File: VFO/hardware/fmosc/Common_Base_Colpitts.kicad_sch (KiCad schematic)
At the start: 28 parts, among them J5 JST PH, J6 3670128, J7 U.FL, Q5 MMBT5179, Q6 MMBT5179, Q7 MMBT5179

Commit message: R1 for generating gerber
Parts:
- removed C16: 10n, g-cap:C_0603_1608Metric, symbol #gplm:cap/CAP-0000-0103
- removed J6: 3670128, g-rfm:H_Wurth_WE-SHC-SEAMLESS-FRAME_3670128, symbol #gplm:rfm/RFM-0000-0001
- added C19: 10n, g-cap:C_0603_1608Metric, symbol #gplm:cap/CAP-0000-0103
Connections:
- net +5V: now also C19.1
- net GND: now also C19.2
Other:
- moved on the sheet: C14, J5, R20

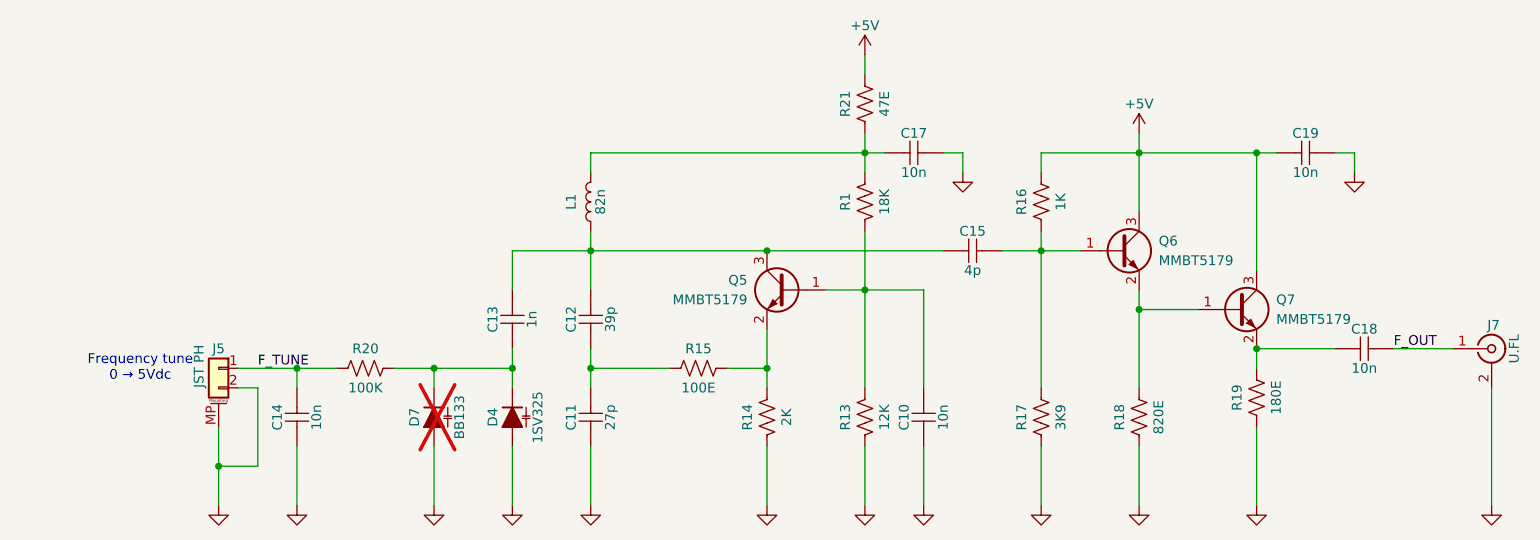
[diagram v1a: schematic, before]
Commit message: Adding DC voltages to the schematic + updating from libraries
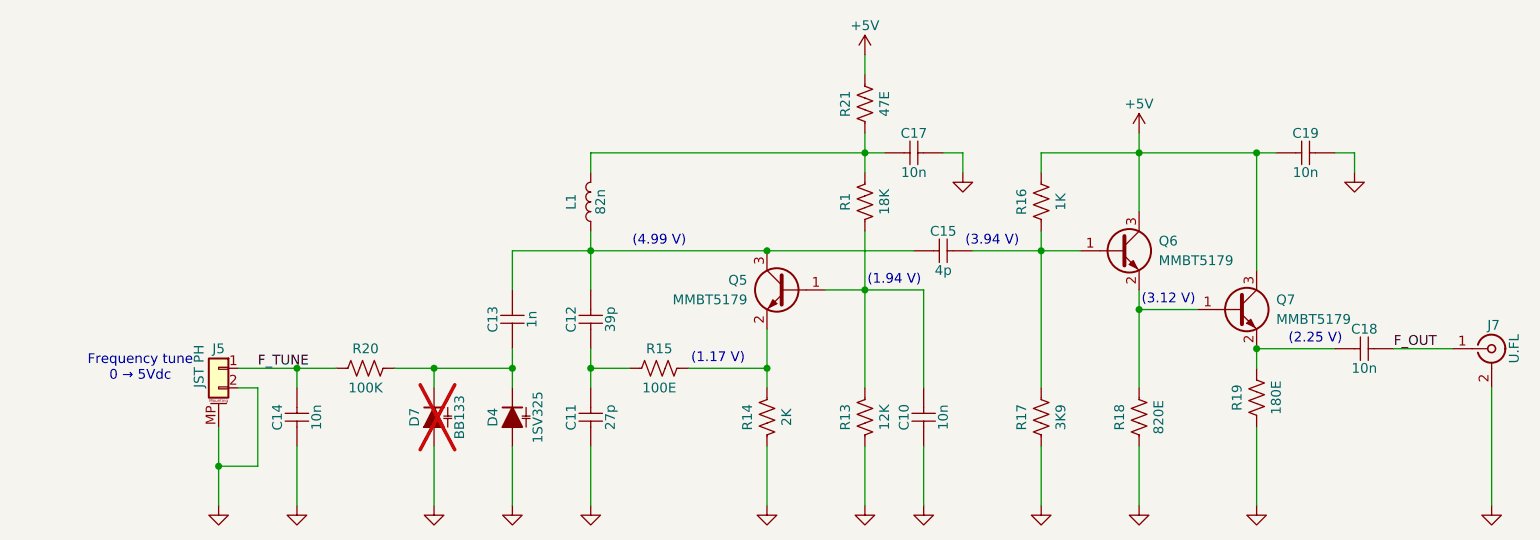
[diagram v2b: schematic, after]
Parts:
- L1: symbol #gplm:ind/IND-0000-0820 -> #gplm:ind/IND-0001-0820; Current 2.5A -> 2.5; IPN IND-0000-0820 -> IND-0001-0820
- Q5, Q6, Q7: max(Ic) 50m -> 0.05
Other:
- note added: "(1.17 V)"
- note added: "(1.94 V)"
- note added: "(2.25 V)"
- note added: "(3.12 V)"
- note added: "(3.94 V)"
- note added: "(4.99 V)"
- moved on the sheet: C15, R15

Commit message: release PBA-0000-0101
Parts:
- C11: value 27p -> 22p; symbol #gplm:cap/CAP-0000-0270 -> #gplm:cap/CAP-0000-0220; Capacitance 27p -> 22p; IPN CAP-0000-0270 -> CAP-0000-0220; LCSC C107045 -> C1653; MPN C0603C270J5GACTU -> CL10C220JB8NNNC; Manufacturer KEMET -> Samsung Electro-Mechanics; Material NP0 -> C0G
- C12: value 39p -> 22p; symbol #gplm:cap/CAP-0000-0390 -> #gplm:cap/CAP-0000-0220; Capacitance 39p -> 22p; IPN CAP-0000-0390 -> CAP-0000-0220; LCSC C107049 -> C1653; MPN C0603C390J5GACTU -> CL10C220JB8NNNC; Manufacturer KEMET -> Samsung Electro-Mechanics; Material NP0 -> C0G
